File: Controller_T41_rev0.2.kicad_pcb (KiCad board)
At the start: 2 copper layers, 102.9 x 69.9 mm, 55 parts, among them J1 8P8C_x4, J2 8P8C_x4, J3 Screw_Terminal_01x02, J4 RJ45_LED, U1 Teensy4.1, U2 AMS1117-5.0, U3 74HC245, U4 74HC245, U5 74HC245, U6 74HC245

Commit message: Updates
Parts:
- moved G*** 0.38 mm to (164.1, 55.8)
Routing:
- net ETH_GND: vias 16 -> 24
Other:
- board text added: "DuotrigesimalWS2811 v0.2 Brian Amos"
- board text added: "JLCJLCJLCJLC"
- board text removed: "DuotrigesimalWS2811"
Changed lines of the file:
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@@
   (general
     (thickness 1.6)
-    (drawings 6)
-    (tracks 523)
+    (drawings 7)
+    (tracks 531)
     (zones 0)
     (modules 55)
@@
   )
   (module Controller_T41_rev0:AC_Logo (layer F.Cu)
-    (at 163.703 55.753)
+    (at 164.084 55.753)
     (fp_text reference G*** (at 0 0) (layer F.SilkS) hide
       (effects (font (size 1.524 1.524) (thickness 0.3)))
@@
     )
   )
-  (gr_text DuotrigesimalWS2811 (at 136.398 53.086) (layer F.SilkS)
+  (gr_text JLCJLCJLCJLC (at 194.818 68.199 90) (layer F.SilkS)
+    (effects (font (size 1.5 1.5) (thickness 0.3)))
+  )
+  (gr_text "DuotrigesimalWS2811 v0.2             Brian Amos" (at 147.574 52.832) (layer F.SilkS)
     (effects (font (size 1 1) (thickness 0.15)))
   )
@@
   (via (at 128.651 77.343) (size 0.8) (drill 0.4) (layers F.Cu B.Cu) (net 1))
   (via (at 128.651 83.185) (size 0.8) (drill 0.4) (layers F.Cu B.Cu) (net 1))
+  (via (at 128.524 56.642) (size 0.8) (drill 0.4) (layers F.Cu B.Cu) (net 1))
+  (via (at 134.239 56.642) (size 0.8) (drill 0.4) (layers F.Cu B.Cu) (net 1))
+  (via (at 131.191 59.69) (size 0.8) (drill 0.4) (layers F.Cu B.Cu) (net 1))
+  (via (at 137.287 59.69) (size 0.8) (drill 0.4) (layers F.Cu B.Cu) (net 1))
+  (via (at 160.147 58.166) (size 0.8) (drill 0.4) (layers F.Cu B.Cu) (net 1))
+  (via (at 117.856 109.474) (size 0.8) (drill 0.4) (layers F.Cu B.Cu) (net 1))
+  (via (at 117.856 113.284) (size 0.8) (drill 0.4) (layers F.Cu B.Cu) (net 1))
+  (via (at 115.697 111.379) (size 0.8) (drill 0.4) (layers F.Cu B.Cu) (net 1))
   (segment (start 166.762 97.409) (end 167.284 97.931) (width 1) (layer F.Cu) (net 2))
   (segment (start 164.685 97.409) (end 166.762 97.409) (width 1) (layer F.Cu) (net 2))
@@
   (segment (start 164.543 90.5805) (end 164.5135 90.551) (width 1) (layer F.Cu) (net 3))
   (segment (start 164.543 94.234) (end 164.543 90.5805) (width 1) (layer F.Cu) (net 3))
-  (segment (start 166.878 86.425) (end 166.878 75.946) (width 0.6) (layer F.Cu) (net 3))
-  (segment (start 173.584 93.131) (end 166.878 86.425) (width 0.6) (layer F.Cu) (net 3))
-  (segment (start 173.584 95.631) (end 173.584 93.131) (width 0.6) (layer F.Cu) (net 3))
+  (segment (start 166.878 86.425) (end 166.878 75.946) (width 1) (layer F.Cu) (net 3))
+  (segment (start 173.584 93.131) (end 166.878 86.425) (width 1) (layer F.Cu) (net 3))
+  (segment (start 173.584 95.631) (end 173.584 93.131) (width 1) (layer F.Cu) (net 3))
   (segment (start 166.878 75.946) (end 172.036 75.946) (width 0.6) (layer F.Cu) (net 3))
   (segment (start 162.736 75.946) (end 166.878 75.946) (width 0.6) (layer F.Cu) (net 3))
   (segment (start 166.878 62.23) (end 167.005 62.103) (width 0.6) (layer F.Cu) (net 3))
-  (segment (start 166.878 75.946) (end 166.878 62.23) (width 0.6) (layer F.Cu) (net 3))
+  (segment (start 166.878 75.946) (end 166.878 62.23) (width 1) (layer F.Cu) (net 3))
   (segment (start 167.005 62.103) (end 172.036 62.103) (width 0.6) (layer F.Cu) (net 3))
   (segment (start 162.736 62.103) (end 167.005 62.103) (width 0.6) (layer F.Cu) (net 3))

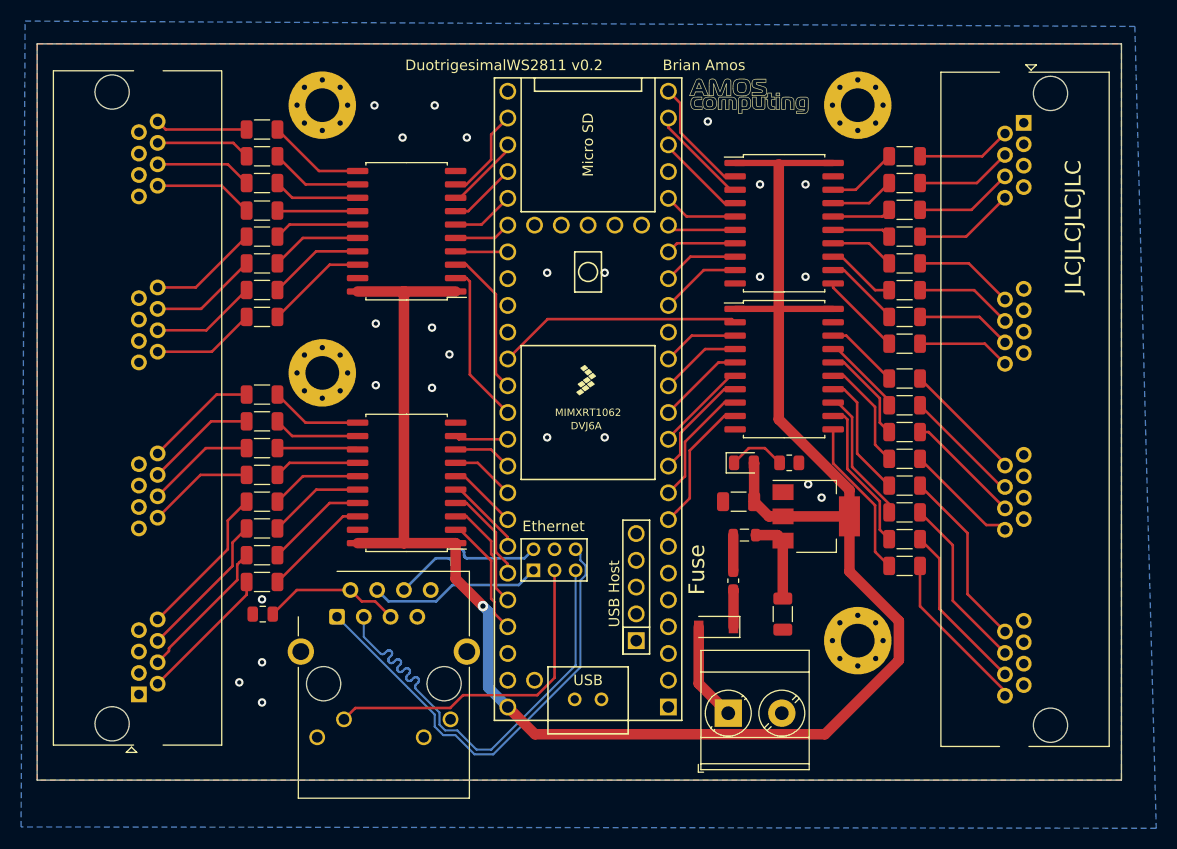
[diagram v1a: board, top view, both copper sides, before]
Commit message: Updated schematic layout and parts. Minor updates to footprint.
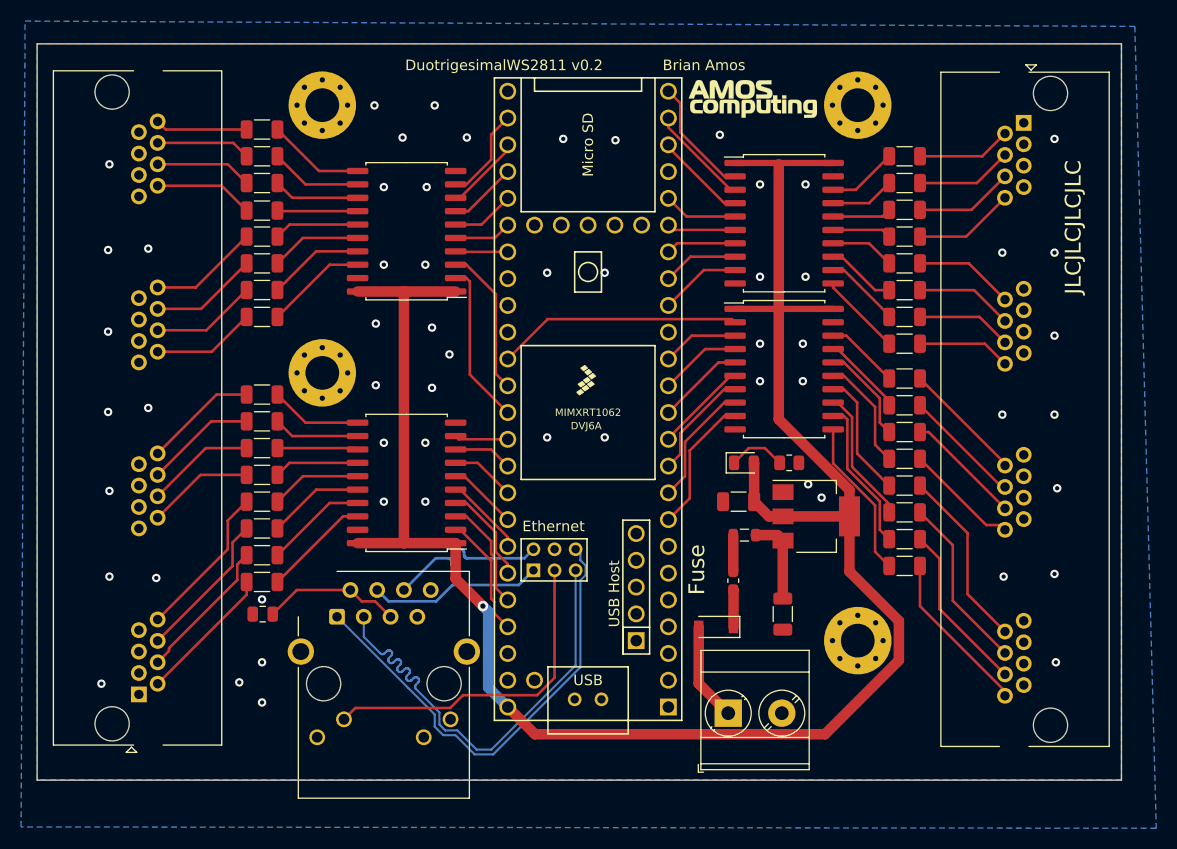
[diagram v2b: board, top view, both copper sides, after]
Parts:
- removed the G*** at (164.1, 55.8)
- added G***: LOGO, Controller_T41_rev0.2:logo, F.Cu at (164.5, 56.0)
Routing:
- net ETH_GND: vias 24 -> 58

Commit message: Updated some parts on LCSC and some smt components
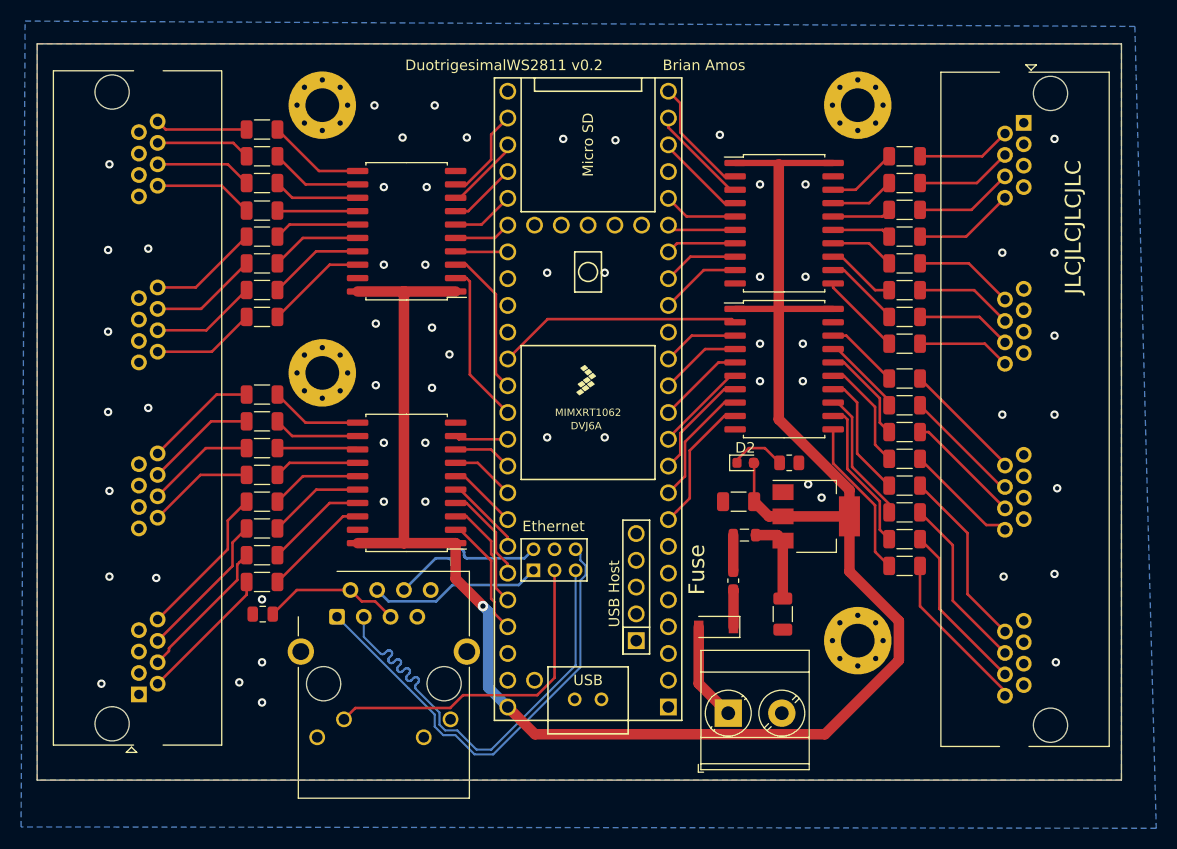
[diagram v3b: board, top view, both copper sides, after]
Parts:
- removed G***: LOGO, Controller_T41_rev0.2:logo
- D2: footprint LED_SMD:LED_0805_2012Metric -> LED_SMD:LED_0603_1608Metric
- U3, U4, U5, U6: value 74HC245 -> 74HCT245
- moved D2 0.13 mm to (163.7, 90.6)

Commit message: Upgraded to Kicad 5.1.9
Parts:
- added G***: LOGO, Controller_T41_rev0.2:logo, F.Cu at (164.3, 56.0)
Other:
- board text added: "1-4"
- board text added: "13-16"
- board text added: "17-20"
- board text added: "21-24"
- board text added: "25-28"
- board text added: "29-32"
- board text added: "5-8"
- board text added: "9-12"

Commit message: Added headers to 3d view
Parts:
- added REF**: PinHeader_1x24_P2.54mm_Vertical, Connector_PinHeader_2.54mm:PinHeader_1x24_P2.54mm_Vertical, F.Cu at (141.2, 113.7)
- added REF**: PinHeader_1x24_P2.54mm_Vertical, Connector_PinHeader_2.54mm:PinHeader_1x24_P2.54mm_Vertical, F.Cu at (156.4, 113.7)
- added REF**: PinHeader_2x03_P2.00mm_Vertical, Connector_PinHeader_2.00mm:PinHeader_2x03_P2.00mm_Vertical, F.Cu at (147.6, 98.8)
